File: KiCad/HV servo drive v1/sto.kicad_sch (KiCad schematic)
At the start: 42 parts, among them J3 Conn_02x03_Top_Bottom, Q1 PMOS, U10 6N137, U11 6N137, U12 FODM217A, U13 FODM217A

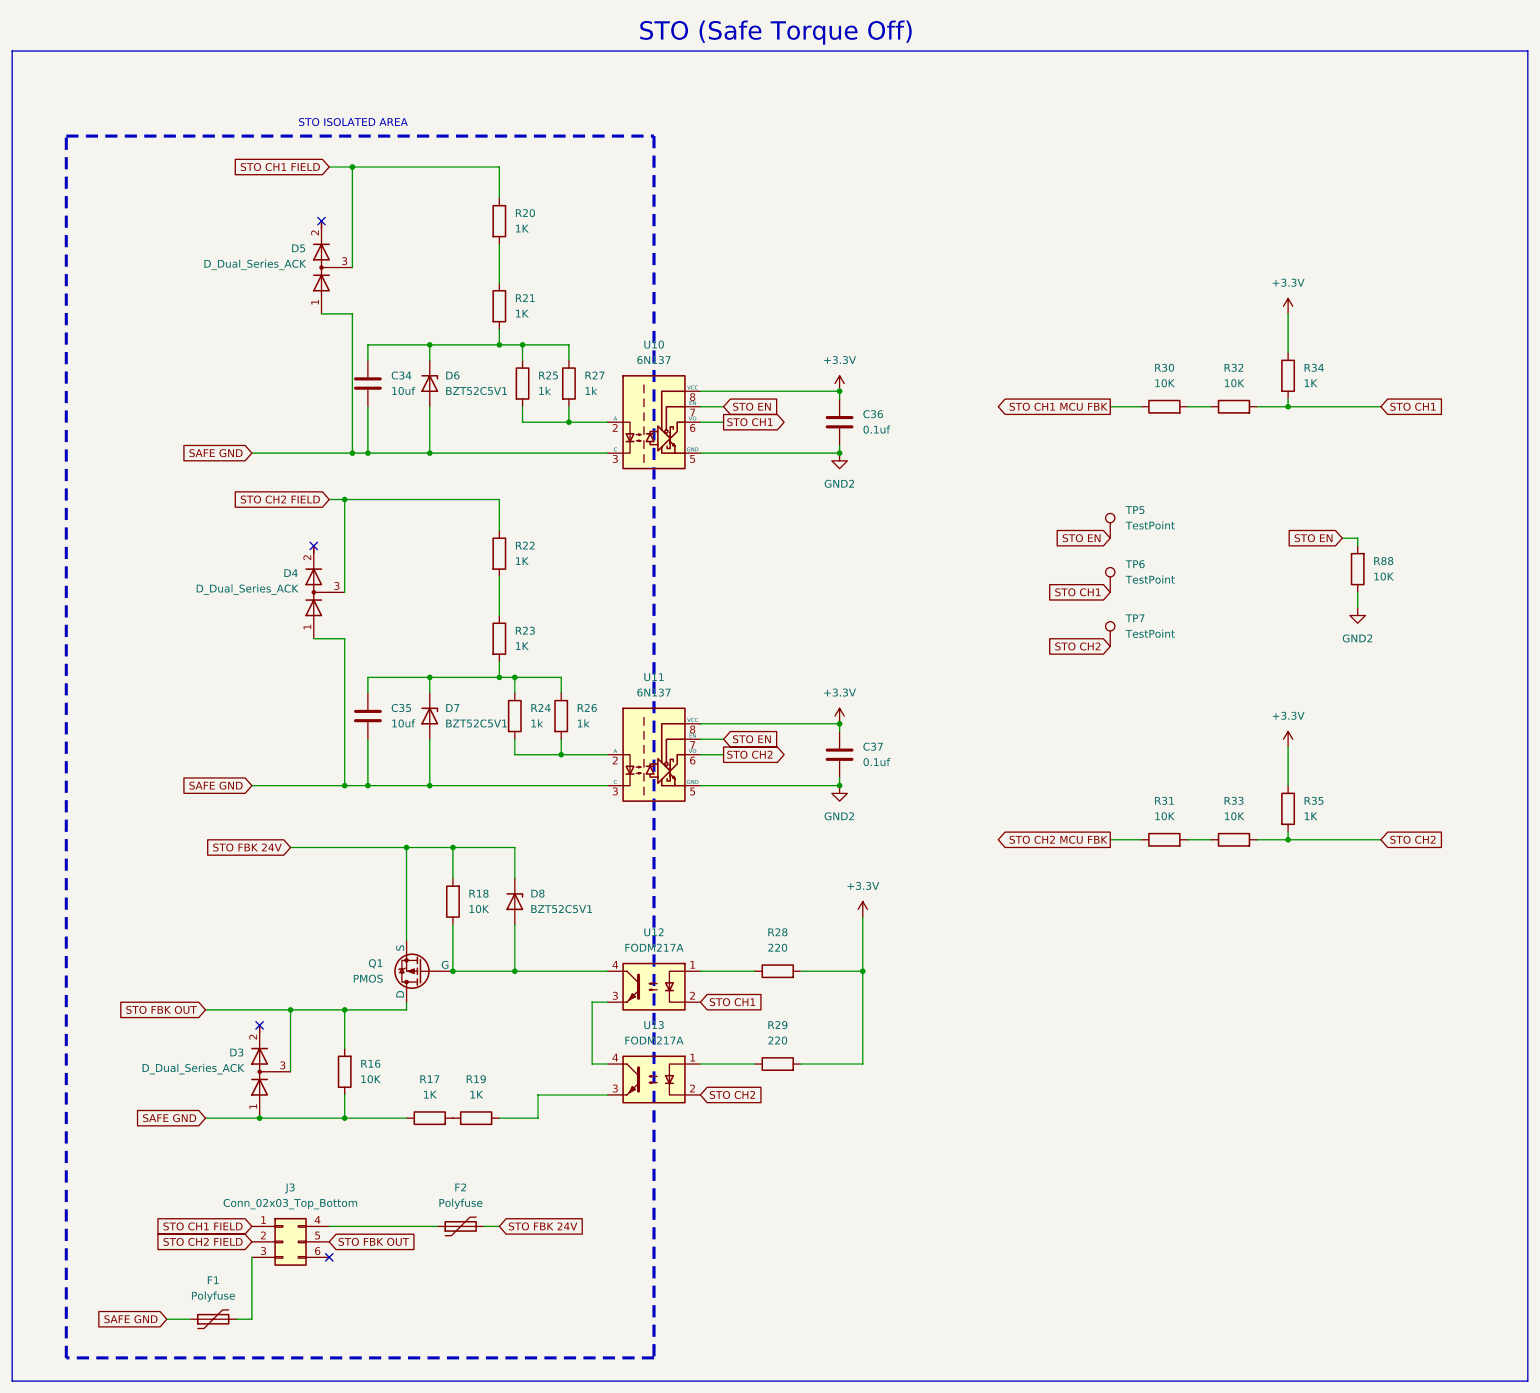
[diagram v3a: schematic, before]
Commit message: update to rev 2.1
basically the same version as in the FOC youtube video, with some minor issues fixed
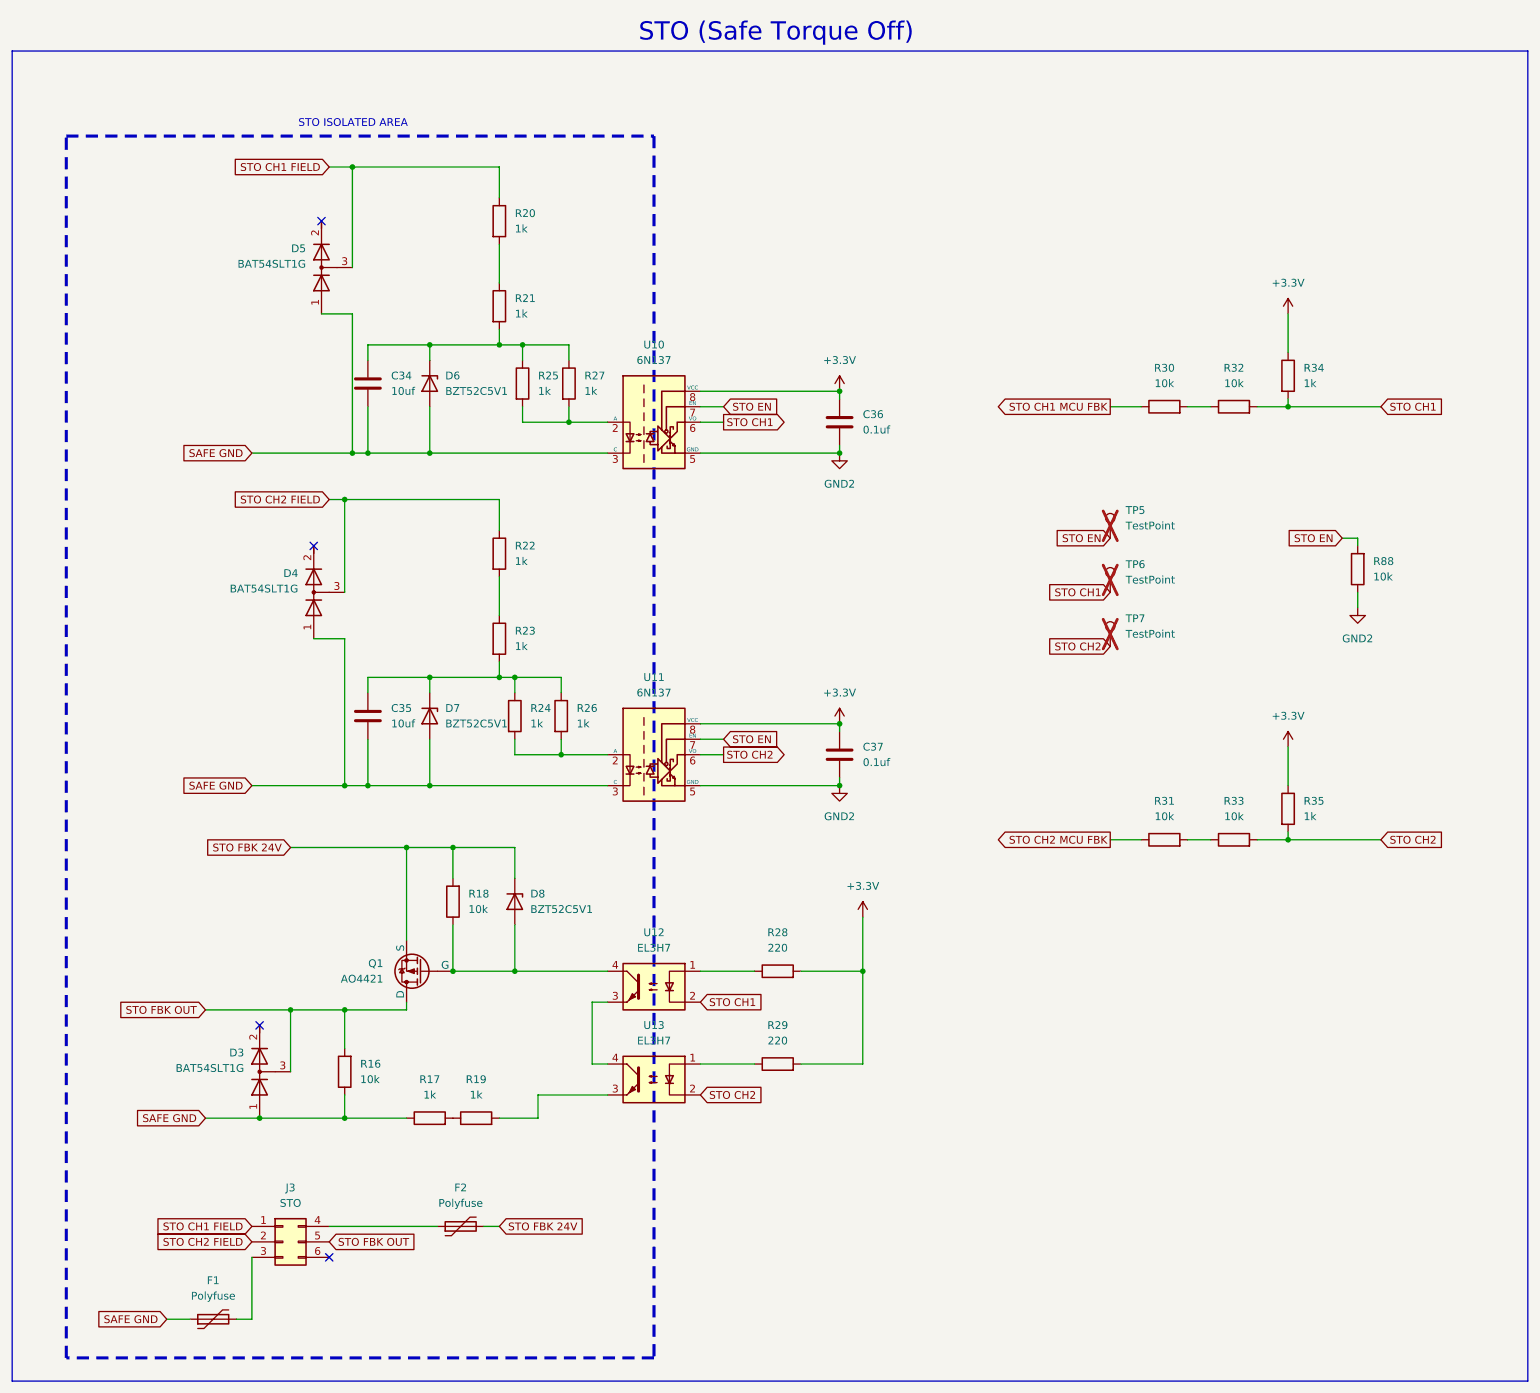
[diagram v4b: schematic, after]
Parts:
- C34, C35: Generic Allowed? (none) -> yes; Manufacturer (none) -> Murata Electronics; Part number (none) -> GRM21BR61H106KE43L
- C36, C37: Generic Allowed? (none) -> yes; Manufacturer (none) -> YAGEO; Part number (none) -> CC0603ZRY5V9BB104
- D3, D4, D5: value D_Dual_Series_ACK -> BAT54SLT1G; Generic Allowed? (none) -> yes; Manufacturer (none) -> onsemi; Part number (none) -> BAT54SLT1G
- D6, D7, D8: Generic Allowed? (none) -> yes; Manufacturer (none) -> Micro Commercial Co; Part number (none) -> BZT52C5V1-TP
- F1, F2: Generic Allowed? (none) -> yes; Manufacturer (none) -> Eaton - Electronics Division; Part number (none) -> PTS120660V005
- J3: value Conn_02x03_Top_Bottom -> STO; footprint Connector_Molex:Molex_Mini-Fit_Jr_5569-06A2_2x03_P4.20mm_Horizontal -> footprints:Molex_Mini-Fit_Jr_0455580003_2x03_P4.20mm_Horizontal; Generic Allowed? (none) -> yes; Manufacturer (none) -> Molex; Part number (none) -> 0455580003
- Q1: value PMOS -> AO4421; Generic Allowed? (none) -> yes; Manufacturer (none) -> Alpha & Omega Semiconductor Inc.; Part number (none) -> AO4421
- R16, R18, R30, R31, R32, R33, R88: value 10K -> 10k; Generic Allowed? (none) -> yes; Manufacturer (none) -> YAGEO; Part number (none) -> RC0603FR-0710KL
- R17, R19, R20, R21, R22, R23, R34, R35: value 1K -> 1k; Generic Allowed? (none) -> yes; Manufacturer (none) -> YAGEO; Part number (none) -> RC0603FR-071KL
- R24, R25, R26, R27: Generic Allowed? (none) -> yes; Manufacturer (none) -> YAGEO; Part number (none) -> RC0603FR-071KL
- R28, R29: Generic Allowed? (none) -> yes; Manufacturer (none) -> YAGEO; Part number (none) -> RC0603FR-07220RL
- TP5, TP6, TP7: now not fitted
- U10, U11: Generic Allowed? (none) -> yes; Manufacturer (none) -> Lite-On Inc.; Part number (none) -> 6N137S-TA1
- U12, U13: value FODM217A -> EL3H7; Generic Allowed? (none) -> yes; Manufacturer (none) -> Everlight Electronics Co Ltd; Part number (none) -> EL3H7(B)(TA)-VG
